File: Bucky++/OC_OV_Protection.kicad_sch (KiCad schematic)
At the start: 44 parts, among them IC10 TPS259830ONRGER, IC7 TPS259830ONRGER, IC8 TPS259830ONRGER, IC9 TPS259830ONRGER

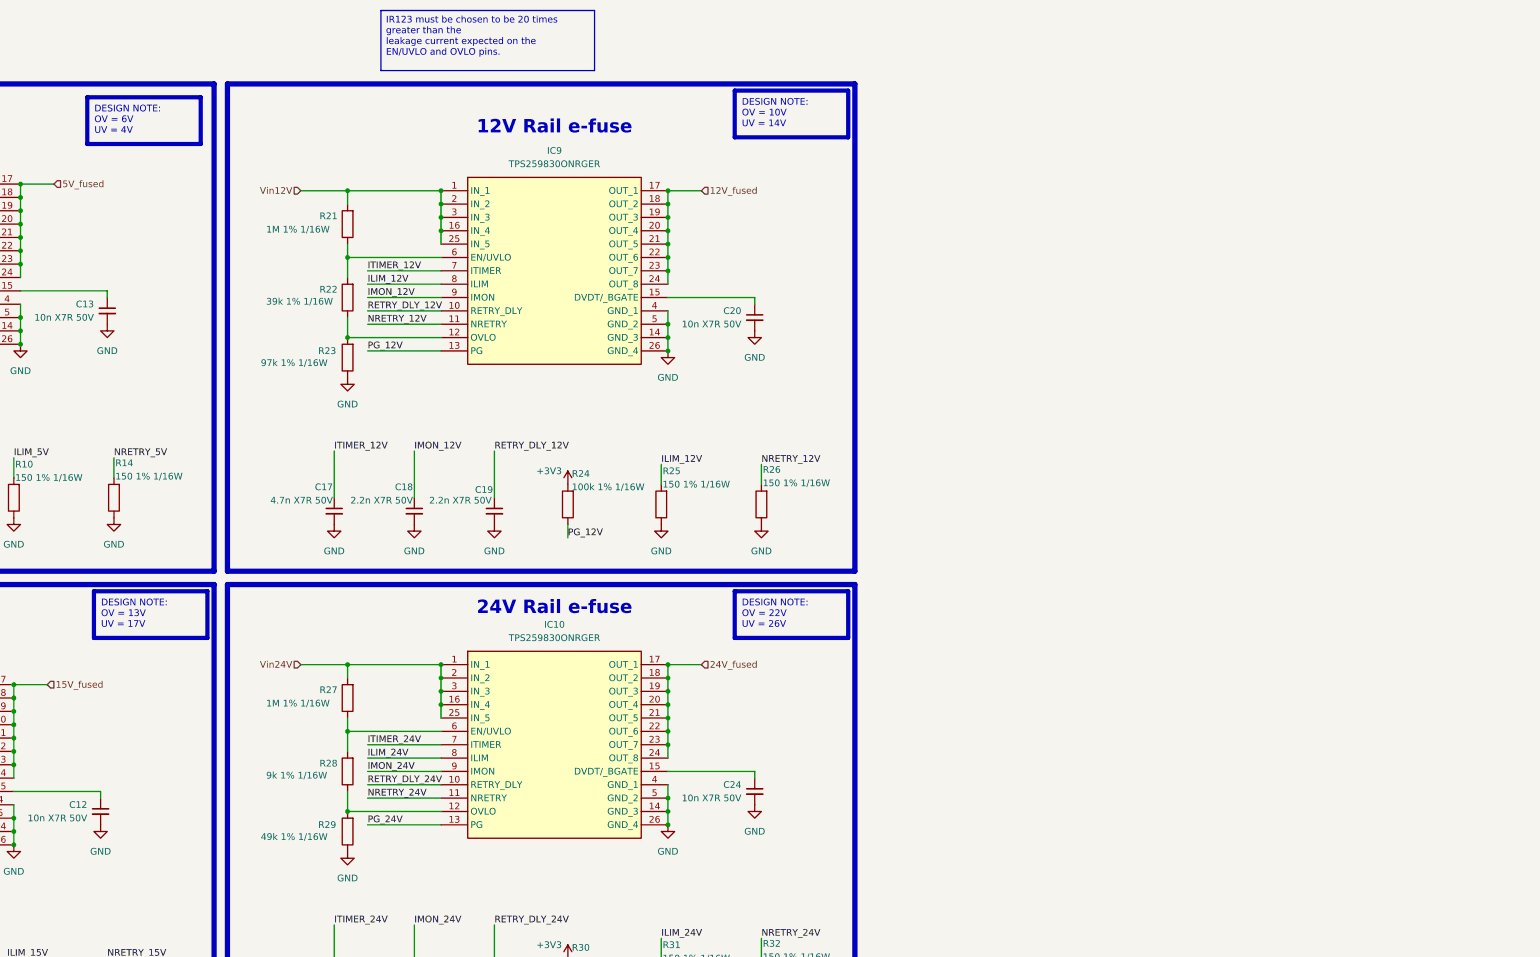
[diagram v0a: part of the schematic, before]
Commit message: added over-current protection on main input
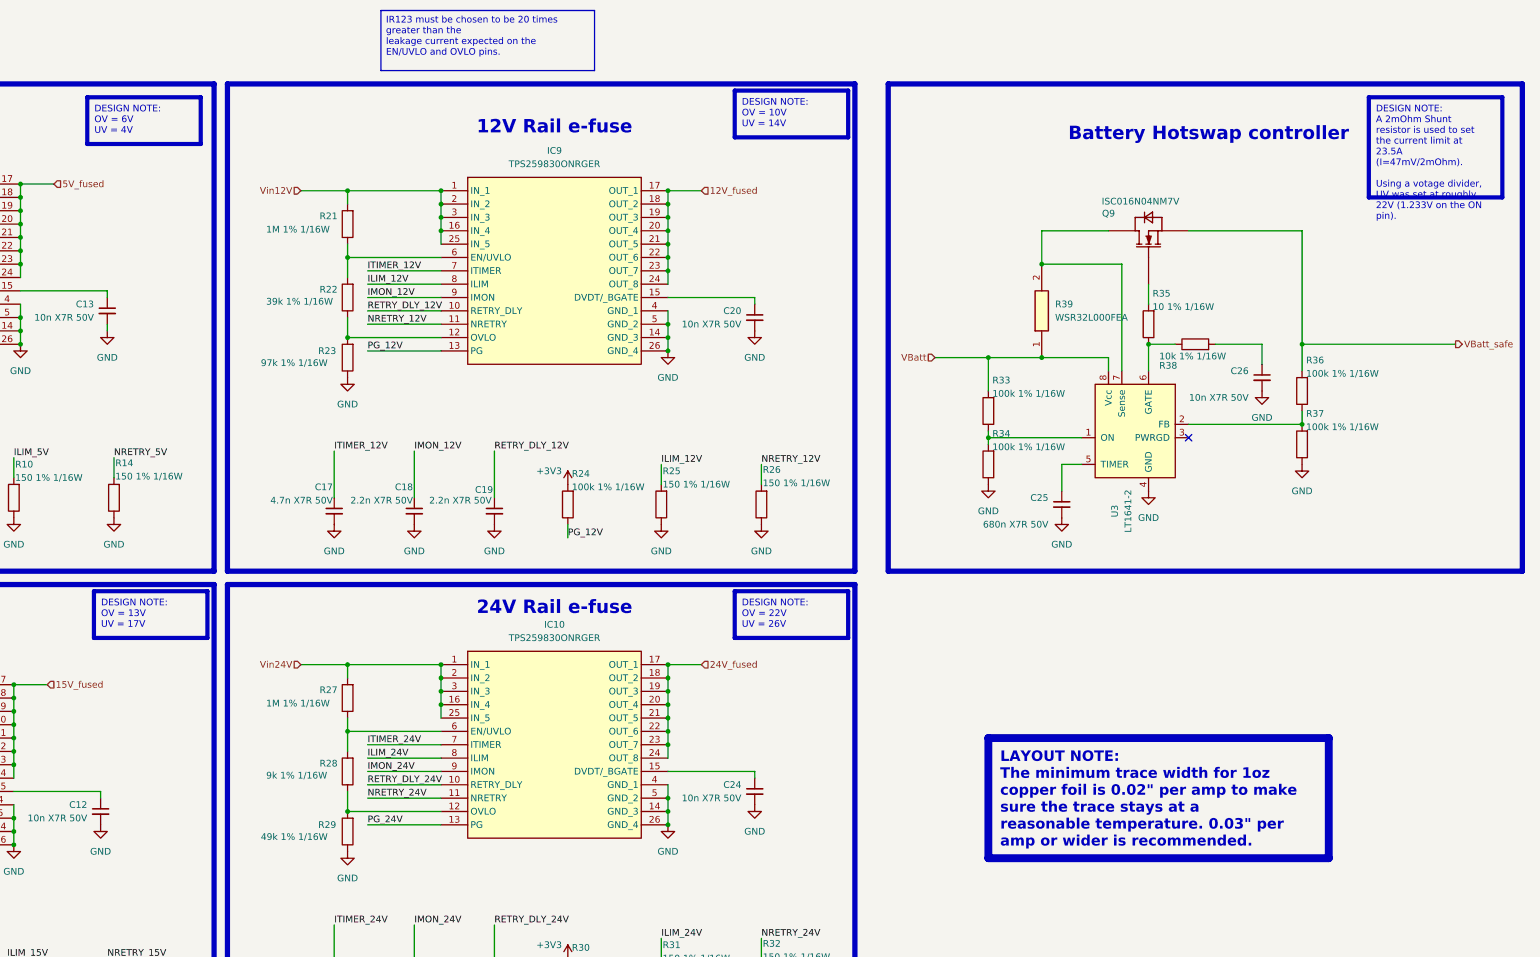
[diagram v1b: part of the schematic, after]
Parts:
- added C25: 680n X7R 50V, 0_capacitor_smd:C_0402_1005_DensityHigh, symbol Device:C_Small
- added C26: 10n X7R 50V, 0_capacitor_smd:C_0402_1005_DensityHigh, symbol Device:C_Small
- added Q9: ISC016N04NM7V, 0_transistor_fet:IFX-PG-TDSON-8-36-V, symbol ISC016N04NM7V:ISC016N04NM7V
- added R33, R34, R36, R37: 100k 1% 1/16W, 0_resistor_smd:R_0402_1005_DensityHigh, symbol Device:R
- added R35: 10 1% 1/16W, 0_resistor_smd:R_0402_1005_DensityHigh, symbol Device:R
- added R38: 10k 1% 1/16W, 0_resistor_smd:R_0402_1005_DensityHigh, symbol Device:R
- added R39: WSR32L000FEA, RESC11670X254N, symbol WSR32L000FEA:WSR32L000FEA
- added U3: LT1641-2, Package_SO:SOIC-8_3.9x4.9mm_P1.27mm, symbol Power_Management:LT1641-2
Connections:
- net GND: now also C25.2, C26.2, R34.1, R37.1, U3.4 (GND)
- new net: C26.1, R38.2
- new net: Q9.5 (DRAIN_1), Q9.6 (DRAIN_2), Q9.7 (DRAIN_3), Q9.8 (DRAIN_4), R39.2, U3.7 (Sense)
- new net: R36.1, R37.2, U3.2 (FB)
- new net: R33.1, R34.2, U3.1 (ON)
- new net: Q9.4 (GATE), R35.2
- new net: R35.1, R38.1, U3.6 (GATE)
- new net: C25.1, U3.5 (TIMER)
- new net VBatt: R33.2, R39.1, U3.8 (Vcc)
- new net VBatt_safe: Q9.1 (SOURCE_1), Q9.2 (SOURCE_2), Q9.3 (SOURCE_3), R36.2
- no-connect marks 0 -> 1

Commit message: fixed errors and added protection diodes
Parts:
- added C27, C28, C29, C30: 100n X7R 50V, 0_capacitor_smd:C_0402_1005_DensityHigh, symbol Device:C_Small
- added D10, D9: B520C-13-F, DIOM7959X250N, symbol SamacSys_Parts:B520C-13-F
- added D12: B530C-13-F, DIOM7959X250N, symbol SamacSys_Parts:B530C-13-F
- added D14: B540C-13-F, DIOM7959X250N, symbol SamacSys_Parts:B540C-13-F
- added D2: SMAT70A-13-F, DIOM5226X230N, symbol SamacSys_Parts:SMAT70A-13-F
- added D3: SMCJ12A, SMCJ12A, symbol SamacSys_Parts:SMCJ12A
- added D4: SMCJ5.0A, SMCJ50A, symbol SamacSys_Parts:SMCJ5.0A
- added D5: SMCJ15A, DIOM7959X262N, symbol SamacSys_Parts:SMCJ15A
- added D6, D8: SMCJ24A, DIONM7959X262N, symbol SamacSys_Parts:SMCJ24A
- added Z1: CMPZ5251B_TR_PBFREE, SOT95P230X109-3N, symbol SamacSys_Parts:CMPZ5251B_TR_PBFREE
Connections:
- net 12V_fused: now also D9.1 (K)
- net 15V_fused: now also D12.1 (K)
- net 24V_fused: now also D14.1 (K)
- net 5V_fused: now also D10.1 (K)
- net GND: now also C27.2, C28.2, C29.2, C30.2, D10.2 (A), D12.2 (A), D14.2 (A), D2.2 (A), D3.2 (A), D4.2 (A), D5.2 (A), D8.2 (A), D9.2 (A)
- net VBatt: now also D2.1 (K)
- net VBatt_safe: now also Z1.1 (ANODE)
- net Vin12V: now also C28.1, D3.1 (K)
- net Vin15V: now also C29.1, D5.1 (K)
- net Vin24V: now also C30.1, D8.1 (K)
- net Vin5V: now also C27.1, D4.1 (K)
- net at R35.1, R38.1, U3.6 (GATE): now also Z1.3 (CATHODE)
- no-connect marks 1 -> 2
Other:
- moved on the sheet: Q9

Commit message: fixed issues after Pedro's review
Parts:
- removed C16, C17, C21, C9: 4.7n X7R 50V, 0_capacitor_smd:C_0402_1005_DensityHigh, symbol Device:C_Small
- removed C23: 2.2n X7R 50V, 0_capacitor_smd:C_0402_1005_DensityHigh, symbol Device:C_Small
- removed D6: SMCJ24A, DIONM7959X262N, symbol SamacSys_Parts:SMCJ24A
- removed R14, R26, R32: 150 1% 1/16W, 0_resistor_smd:R_0402_1005_DensityHigh, symbol Device:R
- removed R39: WSR32L000FEA, RESC11670X254N, symbol WSR32L000FEA:WSR32L000FEA
- added C31: 47n X7R 50V, 0_capacitor_smd:C_0402_1005_DensityHigh, symbol Device:C_Small
- added R39: WSL39211L000JEA, WSL39211L000JEA, symbol SamacSys_Parts:WSL39211L000JEA
- added R40, R41, R42: 500 1% 1/16W, 0_resistor_smd:R_0402_1005_DensityHigh, symbol Device:R
- C10, C11, C15, C18: value 2.2n X7R 50V -> 22n X7R 50V
- C14, C19, C22: value 2.2n X7R 50V -> 47n X7R 50V
- C25: value 680n X7R 50V -> 68n X7R 50V
- R20: value 150 1% 1/16W -> 500 1% 1/16W
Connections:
- net GND: now also C31.2, R40.1, R41.1, R42.1
- net IMON_12V: now also R41.2; no longer C18.1
- net IMON_15V: now also R20.2; no longer C10.1
- net IMON_24V: now also R42.2; no longer C22.1
- net IMON_5V: now also R40.2; no longer C14.1
- net NRETRY_12V: now also C19.1
- net NRETRY_15V: now also C31.1; no longer R20.2
- net NRETRY_24V: now also C14.1
- net NRETRY_5V: now also C22.1
- net RETRY_DLY_12V: now also C18.1; no longer C19.1
- net RETRY_DLY_24V: now also C10.1
- net VBatt: now also R39.1
- net at IC8.15 (DVDT/_BGATE): now also C20.1; no longer C12.1
- net at Q9.5 (DRAIN_1), Q9.6 (DRAIN_2), Q9.7 (DRAIN_3)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: now also R39.2
- net at IC9.15 (DVDT/_BGATE): now also C12.1; no longer C20.1
- no-connect marks 2 -> 6
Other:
- title: (none) -> OC_OV_Protection
- moved on the sheet: C11, C13, C27, D10, D4, IC7, R10, R11, R12, R13, R16, R17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

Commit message: final version before review
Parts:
- C26: value 10n X7R 50V -> 2.2n X7R 50V
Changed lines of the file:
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@@
 		)
 	)
-	(text_box "DESIGN NOTE:\nA current slew rate can be set by limiting the input current at I_INRUSH = CL • 10µA/C26\nHere we set it at x.xA.\n\nA timer during which the max current is exceeded can be set using the formula: C(nF) = 62 • t(ms)\nHere we set it at 1ms"
+	(text_box "DESIGN NOTE:\nA current slew rate can be set by limiting the input current at I_INRUSH = CL • 10µA/C26\nWith CL being the capacitance on the Nav Board (2*68uF = 136uF)\nHere we set it at 0.62A.\n\nA timer during which the max current is exceeded can be set using the formula: C(nF) = 62 • t(ms)\nHere we set it at 1ms"
 		(exclude_from_sim no)
 		(at 384.81 43.18 0)
-		(size 21.59 31.75)
+		(size 21.59 43.18)
 		(margins 1.3525 1.3525 1.3525 1.3525)
 		(stroke
@@
 	(text_box "DESIGN NOTE:\nA 1mOhm Shunt resistor is used to set the current limit at 47A (I=47mV/1mOhm).\n\nUsing a votage divider, UV was set at roughly 22V (1.233V on the ON pin)."
 		(exclude_from_sim no)
-		(at 384.81 77.47 0)
+		(at 384.81 88.9 0)
 		(size 21.59 24.13)
 		(margins 1.3525 1.3525 1.3525 1.3525)
@@
 			)
 		)
-		(property "Value" "10n X7R 50V"
+		(property "Value" "2.2n X7R 50V"
 			(at 330.2 102.87 0)
 			(effects

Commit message: worked on layout, added adm1270
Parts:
- added U4: ADM1270ACPZ, Package_CSP:LFCSP-16-1EP_3x3mm_P0.5mm_EP1.5x1.5mm, symbol Power_Management:ADM1270ACPZ
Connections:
- net VBatt: no longer R39.1
- net VBatt_safe: no longer Q9.1 (SOURCE_1), Q9.2 (SOURCE_2), Q9.3 (SOURCE_3)
- net at Q9.5 (DRAIN_1), Q9.6 (DRAIN_2), Q9.7 (DRAIN_3)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: now also U4.14 (SENSE-); no longer U3.7 (Sense)
- net at Q9.4 (GATE): now also U4.13 (GATE); no longer R35.2
- new net: U4.1 (VCAP), U4.2 (ISET)
- new net: R39.1, U4.15 (VCC)
- new net: U4.17 (EP), U4.7 (GND)
- new net: U4.5 (ENABLE), U4.6 (~{FAULT})
- new net: Q9.1 (SOURCE_1), Q9.2 (SOURCE_2), Q9.3 (SOURCE_3)
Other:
- moved on the sheet: Q9, R39

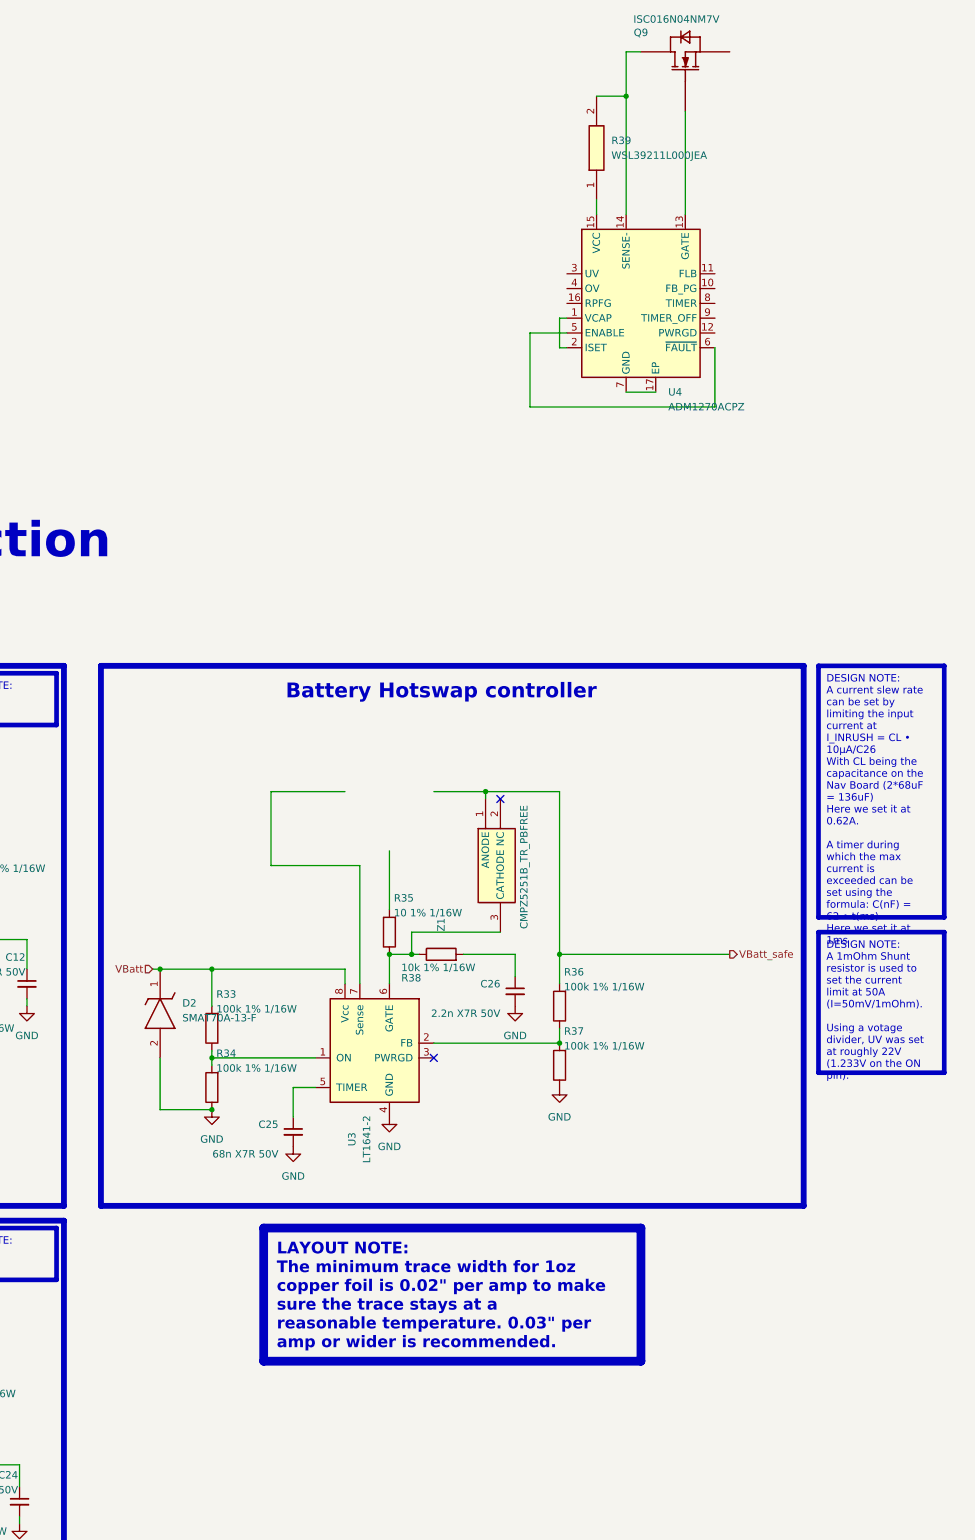
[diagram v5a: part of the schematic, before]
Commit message: implemented ADM1270 (no foldback yet
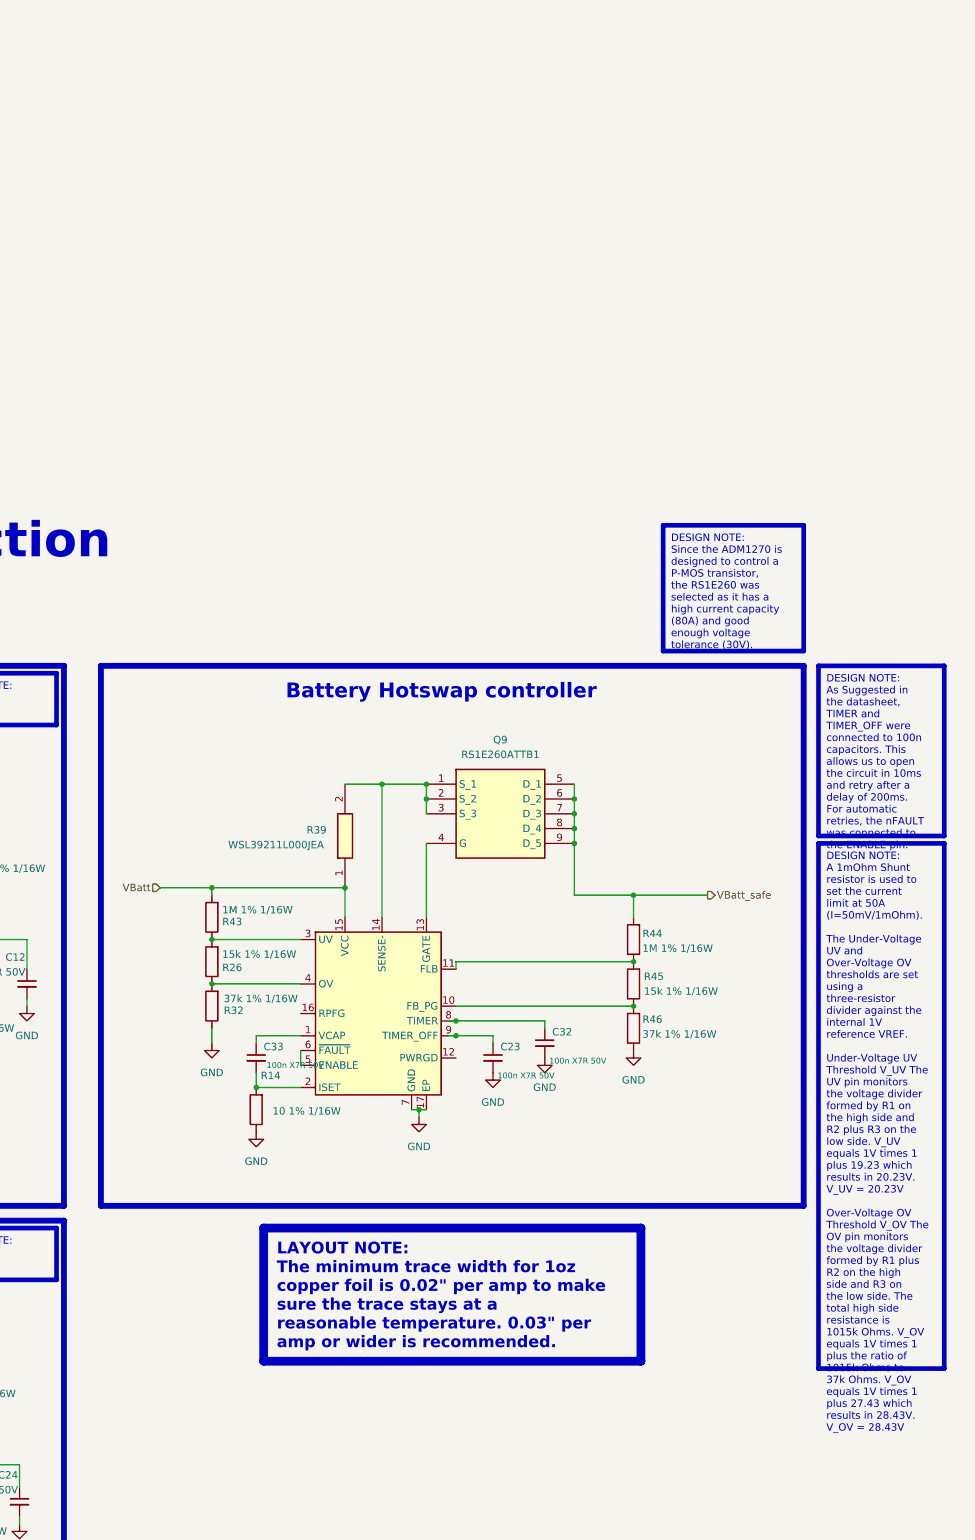
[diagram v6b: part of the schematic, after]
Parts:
- removed C25: 68n X7R 50V, 0_capacitor_smd:C_0402_1005_DensityHigh, symbol Device:C_Small
- removed C26: 2.2n X7R 50V, 0_capacitor_smd:C_0402_1005_DensityHigh, symbol Device:C_Small
- removed D2: SMAT70A-13-F, DIOM5226X230N, symbol SamacSys_Parts:SMAT70A-13-F
- removed Q9: ISC016N04NM7V, 0_transistor_fet:IFX-PG-TDSON-8-36-V, symbol ISC016N04NM7V:ISC016N04NM7V
- removed R33, R34, R36, R37: 100k 1% 1/16W, 0_resistor_smd:R_0402_1005_DensityHigh, symbol Device:R
- removed R35: 10 1% 1/16W, 0_resistor_smd:R_0402_1005_DensityHigh, symbol Device:R
- removed R38: 10k 1% 1/16W, 0_resistor_smd:R_0402_1005_DensityHigh, symbol Device:R
- removed U3: LT1641-2, Package_SO:SOIC-8_3.9x4.9mm_P1.27mm, symbol Power_Management:LT1641-2
- removed Z1: CMPZ5251B_TR_PBFREE, SOT95P230X109-3N, symbol SamacSys_Parts:CMPZ5251B_TR_PBFREE
- added C23, C32, C33: 100n X7R 50V, 0_capacitor_smd:C_0402_1005_DensityHigh, symbol Device:C_Small
- added Q9: RS1E260ATTB1, RS1E260ATTB1, symbol SamacSys_Parts:RS1E260ATTB1
- added R14: 10 1% 1/16W, 0_resistor_smd:R_0402_1005_DensityHigh, symbol Device:R
- added R26, R45: 15k 1% 1/16W, 0_resistor_smd:R_0402_1005_DensityHigh, symbol Device:R
- added R32, R46: 37k 1% 1/16W, 0_resistor_smd:R_0402_1005_DensityHigh, symbol Device:R
- added R43, R44: 1M 1% 1/16W, 0_resistor_smd:R_0402_1005_DensityHigh, symbol Device:R
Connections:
- net GND: now also U4.17 (EP), U4.7 (GND), C23.2, C32.2, R14.1, R32.1, R46.1
- net VBatt: now also R39.1, U4.15 (VCC), R43.2
- net VBatt_safe: now also Q9.5 (D_1), Q9.6 (D_2), Q9.7 (D_3), Q9.8 (D_4), Q9.9 (D_5), R44.2
- net at U4.1 (VCAP): now also C33.1; no longer U4.2 (ISET)
- net at U4.10 (FB_PG): now also R45.1, R46.2
- net at U4.11 (FLB): now also R44.1, R45.2
- net at U4.13 (GATE): now also Q9.4 (G)
- net at R39.2, U4.14 (SENSE-): now also Q9.1 (S_1), Q9.2 (S_2), Q9.3 (S_3)
- net at U4.3 (UV): now also R26.2, R43.1
- net at U4.4 (OV): now also R26.1, R32.2
- net at U4.8 (TIMER): now also C32.1
- net at U4.9 (TIMER_OFF): now also C23.1
- new net: C33.2, R14.2, U4.2 (ISET)
- no-connect marks 6 -> 4
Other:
- moved on the sheet: R39

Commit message: implemented foldback
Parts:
- removed R45: 15k 1% 1/16W, 0_resistor_smd:R_0402_1005_DensityHigh, symbol Device:R
- added R33: 2.3k 1% 1/16W, 0_resistor_smd:R_0402_1005_DensityHigh, symbol Device:R
- added R34: 15k 1% 1/16W, 0_resistor_smd:R_0402_1005_DensityHigh, symbol Device:R
- R14: value 10 1% 1/16W -> 3.6k 1% 1/16W
- R46: value 37k 1% 1/16W -> 133k 1% 1/16W
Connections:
- net GND: now also C33.2, R33.1; no longer R14.1
- net at C33.1, U4.1 (VCAP): now also R14.2, R34.2
- net at U4.10 (FB_PG): no longer R46.2
- net at R44.1, U4.11 (FLB): now also R46.2
- net at U4.5 (ENABLE), U4.6 (~{FAULT}): now also R34.1
- new net: R14.1, R33.2, U4.2 (ISET)
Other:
- moved on the sheet: C23, C32, C33, Q9, R26, R32, R39, R43, R44, R46
